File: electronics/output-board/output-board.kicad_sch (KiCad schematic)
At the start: 30 parts, among them J14 Arming switch, J19 Extra IO, J3 12V In, J4 Conn_01x02, J5 SWD Header, J6 Conn_01x02, SW1 SW_Push_Dual, U1 MAX33012EASA+, U2 LD3985M33R_SOT23, U3 STM32F105VBH6, Y1 25MHz 9pF

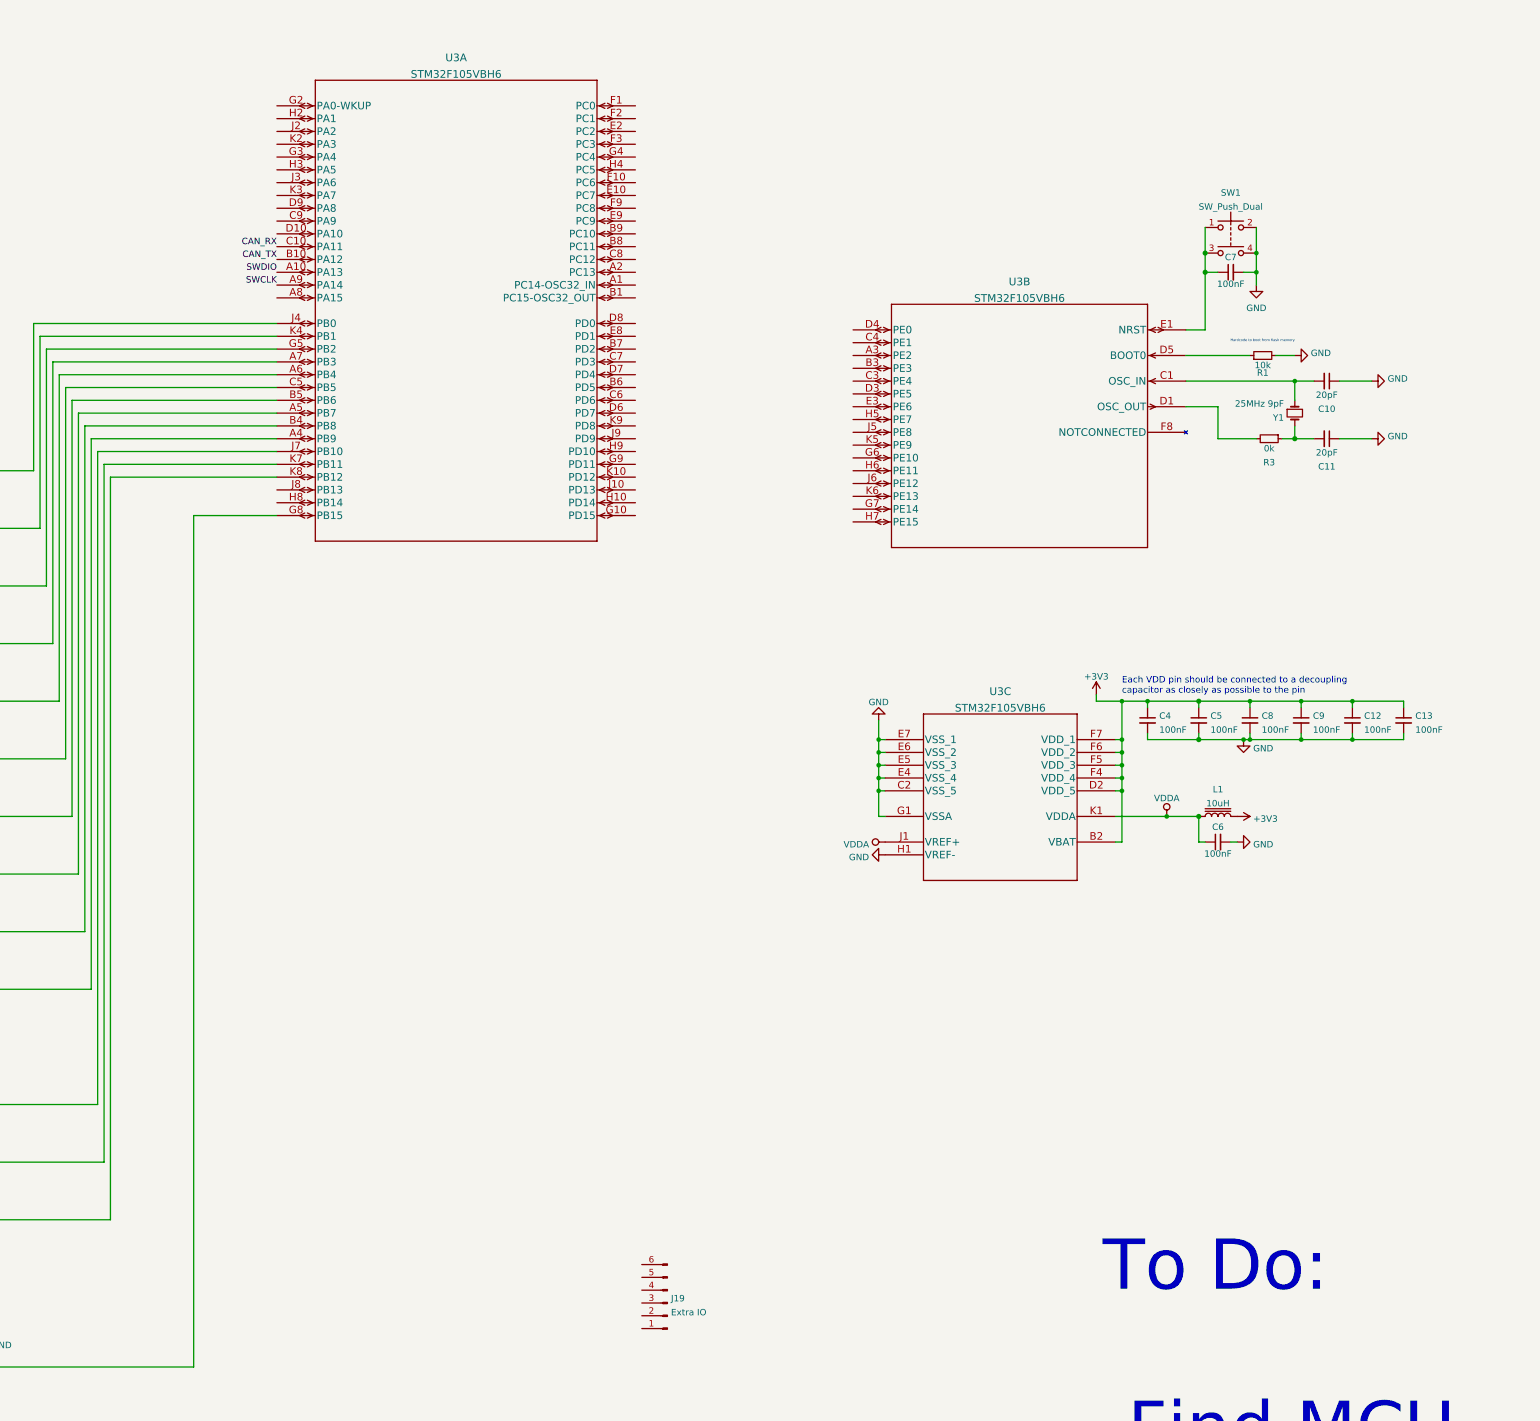
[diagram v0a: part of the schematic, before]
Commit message: Continued Laying Out Output Board
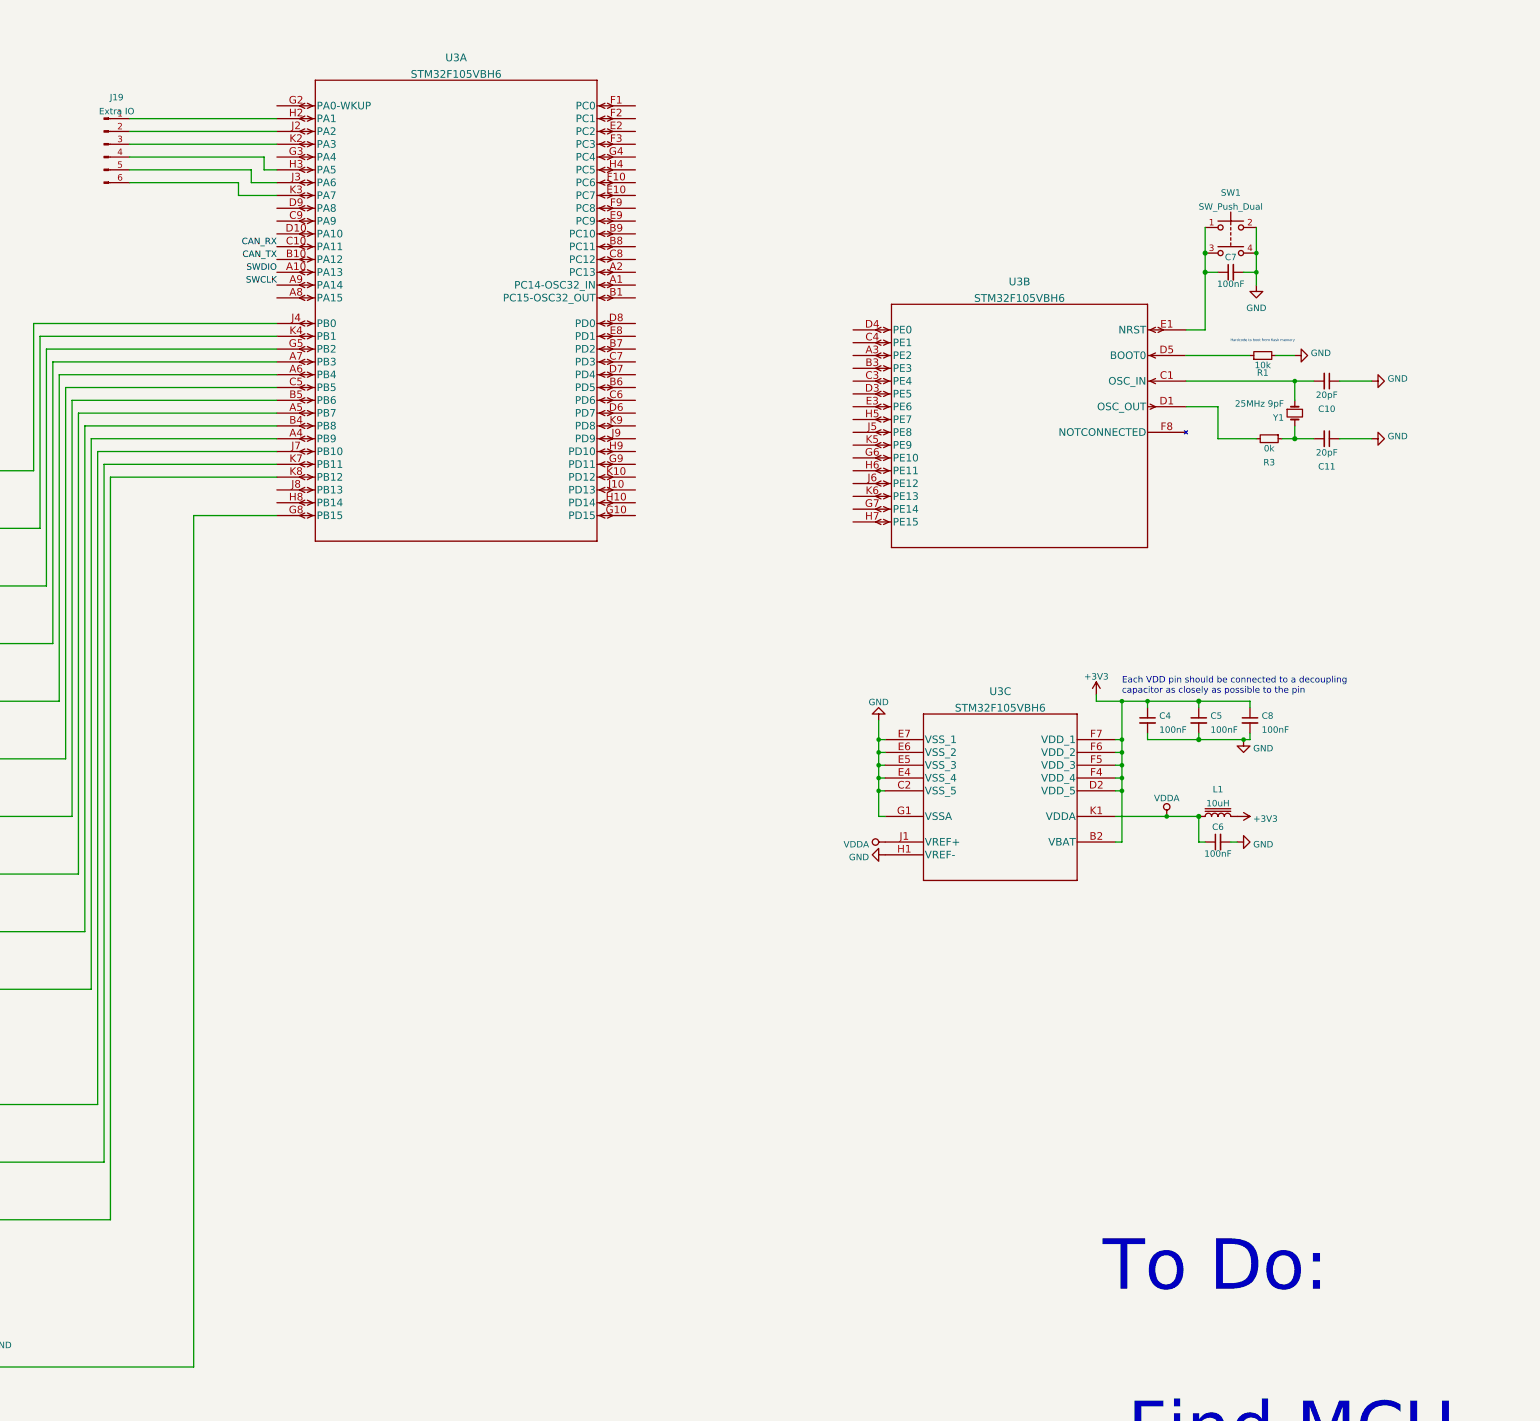
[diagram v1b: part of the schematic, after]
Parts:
- removed C12, C13, C9: 100nF, Capacitor_SMD:C_0603_1608Metric, symbol Device:C_Small
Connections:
- net at J19.1 (Pin_1): now also U3.H2 (PA1)
- net at J19.2 (Pin_2): now also U3.J2 (PA2)
- net at J19.3 (Pin_3): now also U3.K2 (PA3)
- net at J19.4 (Pin_4): now also U3.H3 (PA5)
- net at J19.5 (Pin_5): now also U3.J3 (PA6)
- net at J19.6 (Pin_6): now also U3.K3 (PA7)
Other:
- moved on the sheet: J19
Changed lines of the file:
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@@
   (junction (at 349.25 101.6) (diameter 1.016) (color 0 0 0 0))
   (junction (at 356.87 194.31) (diameter 0) (color 0 0 0 0))
-  (junction (at 358.14 186.69) (diameter 0) (color 0 0 0 0))
-  (junction (at 358.14 194.31) (diameter 0) (color 0 0 0 0))
   (junction (at 359.41 97.79) (diameter 0) (color 0 0 0 0))
   (junction (at 359.41 101.6) (diameter 0) (color 0 0 0 0))
   (junction (at 367.03 123.19) (diameter 0) (color 0 0 0 0))
   (junction (at 367.03 134.62) (diameter 1.016) (color 0 0 0 0))
-  (junction (at 368.3 186.69) (diameter 0) (color 0 0 0 0))
-  (junction (at 368.3 194.31) (diameter 0) (color 0 0 0 0))
-  (junction (at 378.46 186.69) (diameter 0) (color 0 0 0 0))
-  (junction (at 378.46 194.31) (diameter 0) (color 0 0 0 0))
   (wire (pts (xy 25.4 81.28) (xy 35.56 81.28))
     (stroke (width 0) (type solid) (color 0 0 0 0))
@@
     (stroke (width 0) (type default) (color 0 0 0 0))
   )
+  (wire (pts (xy 135.89 71.12) (xy 165.1 71.12))
+    (stroke (width 0) (type default) (color 0 0 0 0))
+  )
+  (wire (pts (xy 135.89 73.66) (xy 165.1 73.66))
+    (stroke (width 0) (type default) (color 0 0 0 0))
+  )
+  (wire (pts (xy 135.89 76.2) (xy 165.1 76.2))
+    (stroke (width 0) (type default) (color 0 0 0 0))
+  )
   (wire (pts (xy 148.59 149.86) (xy 148.59 318.77))
     (stroke (width 0) (type default) (color 0 0 0 0))
   )
+  (wire (pts (xy 157.48 83.82) (xy 135.89 83.82))
+    (stroke (width 0) (type default) (color 0 0 0 0))
+  )
+  (wire (pts (xy 157.48 86.36) (xy 157.48 83.82))
+    (stroke (width 0) (type default) (color 0 0 0 0))
+  )
+  (wire (pts (xy 160.02 81.28) (xy 135.89 81.28))
+    (stroke (width 0) (type default) (color 0 0 0 0))
+  )
+  (wire (pts (xy 160.02 83.82) (xy 160.02 81.28))
+    (stroke (width 0) (type default) (color 0 0 0 0))
+  )
+  (wire (pts (xy 162.56 78.74) (xy 135.89 78.74))
+    (stroke (width 0) (type default) (color 0 0 0 0))
+  )
+  (wire (pts (xy 162.56 81.28) (xy 162.56 78.74))
+    (stroke (width 0) (type default) (color 0 0 0 0))
+  )
+  (wire (pts (xy 165.1 81.28) (xy 162.56 81.28))
+    (stroke (width 0) (type default) (color 0 0 0 0))
+  )
+  (wire (pts (xy 165.1 83.82) (xy 160.02 83.82))
+    (stroke (width 0) (type default) (color 0 0 0 0))
+  )
+  (wire (pts (xy 165.1 86.36) (xy 157.48 86.36))
+    (stroke (width 0) (type default) (color 0 0 0 0))
+  )
   (wire (pts (xy 165.1 114.3) (xy 118.11 114.3))
     (stroke (width 0) (type default) (color 0 0 0 0))
@@
     (stroke (width 0) (type solid) (color 0 0 0 0))
   )
-  (wire (pts (xy 358.14 186.69) (xy 368.3 186.69))
-    (stroke (width 0) (type default) (color 0 0 0 0))
-  )
   (wire (pts (xy 358.14 193.04) (xy 358.14 194.31))
     (stroke (width 0) (type solid) (color 0 0 0 0))
@@
     (stroke (width 0) (type solid) (color 0 0 0 0))
   )
-  (wire (pts (xy 368.3 187.96) (xy 368.3 186.69))
-    (stroke (width 0) (type default) (color 0 0 0 0))
-  )
-  (wire (pts (xy 368.3 193.04) (xy 368.3 194.31))
-    (stroke (width 0) (type default) (color 0 0 0 0))
-  )
-  (wire (pts (xy 368.3 194.31) (xy 358.14 194.31))
-    (stroke (width 0) (type default) (color 0 0 0 0))
-  )
-  (wire (pts (xy 368.3 194.31) (xy 378.46 194.31))
-    (stroke (width 0) (type default) (color 0 0 0 0))
-  )
   (wire (pts (xy 370.84 123.19) (xy 367.03 123.19))
     (stroke (width 0) (type solid) (color 0 0 0 0))
@@
     (stroke (width 0) (type solid) (color 0 0 0 0))
   )
-  (wire (pts (xy 378.46 186.69) (xy 368.3 186.69))
-    (stroke (width 0) (type default) (color 0 0 0 0))
-  )
-  (wire (pts (xy 378.46 186.69) (xy 388.62 186.69))
-    (stroke (width 0) (type default) (color 0 0 0 0))
-  )
-  (wire (pts (xy 378.46 187.96) (xy 378.46 186.69))
-    (stroke (width 0) (type default) (color 0 0 0 0))
-  )
-  (wire (pts (xy 378.46 193.04) (xy 378.46 194.31))
-    (stroke (width 0) (type default) (color 0 0 0 0))
-  )
-  (wire (pts (xy 378.46 194.31) (xy 388.62 194.31))
-    (stroke (width 0) (type default) (color 0 0 0 0))
-  )
   (wire (pts (xy 382.27 123.19) (xy 375.92 123.19))
     (stroke (width 0) (type solid) (color 0 0 0 0))
@@
   (wire (pts (xy 382.27 134.62) (xy 375.92 134.62))
     (stroke (width 0) (type solid) (color 0 0 0 0))
-  )
-  (wire (pts (xy 388.62 187.96) (xy 388.62 186.69))
-    (stroke (width 0) (type default) (color 0 0 0 0))
-  )
-  (wire (pts (xy 388.62 193.04) (xy 388.62 194.31))
-    (stroke (width 0) (type default) (color 0 0 0 0))
   )
   (text "To Do:\n\n-Find MCU\n-Add IO Breakout\n-Finalize Connectors\n-Put together final parrts list\n-Buy parts and board"
@@
     (pin "2")
   )
-  (symbol (lib_id "Device:C_Small") (at 368.3 190.5 0) (unit 1)
-    (in_bom yes) (on_board yes)
-    (property "Reference" "C9" (id 0) (at 370.6242 189.5915 0)
-      (effects (font (size 1.27 1.27)) (justify left))
-    )
-    (property "Value" "100nF" (id 1) (at 370.6242 192.3666 0)
-      (effects (font (size 1.27 1.27)) (justify left))
-    )
-    (property "Footprint" "Capacitor_SMD:C_0603_1608Metric" (id 2) (at 368.3 190.5 0)
-      (effects (font (size 1.27 1.27)) hide)
-    )
-    (property "Datasheet" "~" (id 3) (at 368.3 190.5 0)
-      (effects (font (size 1.27 1.27)) hide)
-    )
-    (pin "1")
-    (pin "2")
-  )
   (symbol (lib_id "Device:C_Small") (at 373.38 123.19 270) (unit 1)
     (in_bom yes) (on_board yes) (fields_autoplaced)
@@
     (pin "2")
   )
-  (symbol (lib_id "Device:C_Small") (at 378.46 190.5 0) (unit 1)
-    (in_bom yes) (on_board yes)
-    (property "Reference" "C12" (id 0) (at 380.7842 189.5915 0)
-      (effects (font (size 1.27 1.27)) (justify left))
-    )
-    (property "Value" "100nF" (id 1) (at 380.7842 192.3666 0)
-      (effects (font (size 1.27 1.27)) (justify left))
-    )
-    (property "Footprint" "Capacitor_SMD:C_0603_1608Metric" (id 2) (at 378.46 190.5 0)
-      (effects (font (size 1.27 1.27)) hide)
-    )
-    (property "Datasheet" "~" (id 3) (at 378.46 190.5 0)
-      (effects (font (size 1.27 1.27)) hide)
-    )
-    (pin "1")
-    (pin "2")
-  )
-  (symbol (lib_id "Device:C_Small") (at 388.62 190.5 0) (unit 1)
-    (in_bom yes) (on_board yes)
-    (property "Reference" "C13" (id 0) (at 390.9442 189.5915 0)
-      (effects (font (size 1.27 1.27)) (justify left))
-    )
-    (property "Value" "100nF" (id 1) (at 390.9442 192.3666 0)
-      (effects (font (size 1.27 1.27)) (justify left))
-    )
-    (property "Footprint" "Capacitor_SMD:C_0603_1608Metric" (id 2) (at 388.62 190.5 0)
-      (effects (font (size 1.27 1.27)) hide)
-    )
-    (property "Datasheet" "~" (id 3) (at 388.62 190.5 0)
-      (effects (font (size 1.27 1.27)) hide)
-    )
-    (pin "1")
-    (pin "2")
-  )
   (symbol (lib_id "Device:R") (at 55.88 299.72 270) (unit 1)
     (in_bom yes) (on_board yes)
@@
     (pin "4")
   )
-  (symbol (lib_id "Connector:Conn_01x06_Male") (at 242.57 306.07 180) (unit 1)
-    (in_bom yes) (on_board yes) (fields_autoplaced)
-    (property "Reference" "J19" (id 0) (at 243.2813 305.1615 0)
-      (effects (font (size 1.27 1.27)) (justify right))
-    )
-    (property "Value" "Extra IO" (id 1) (at 243.2813 307.9366 0)
-      (effects (font (size 1.27 1.27)) (justify right))
-    )
-    (property "Footprint" "Connector_PinHeader_2.54mm:PinHeader_2x03_P2.54mm_Vertical" (id 2) (at 242.57 306.07 0)
-      (effects (font (size 1.27 1.27)) hide)
-    )
-    (property "Datasheet" "~" (id 3) (at 242.57 306.07 0)
+  (symbol (lib_id "Connector:Conn_01x06_Male") (at 130.81 76.2 0) (unit 1)
+    (in_bom yes) (on_board yes) (fields_autoplaced)
+    (property "Reference" "J19" (id 0) (at 133.3119 66.8994 0))
+    (property "Value" "Extra IO" (id 1) (at 133.3119 69.6745 0))
+    (property "Footprint" "Connector_PinHeader_2.54mm:PinHeader_2x03_P2.54mm_Vertical" (id 2) (at 130.81 76.2 0)
+      (effects (font (size 1.27 1.27)) hide)
+    )
+    (property "Datasheet" "~" (id 3) (at 130.81 76.2 0)
       (effects (font (size 1.27 1.27)) hide)
     )
@@
       (reference "C8") (unit 1) (value "100nF") (footprint "Capacitor_SMD:C_0603_1608Metric")
     )
-    (path "/6c7ff70a-85ef-4e9c-b06b-8c61c0a8b9d8"
-      (reference "C9") (unit 1) (value "100nF") (footprint "Capacitor_SMD:C_0603_1608Metric")
-    )
     (path "/a4541931-eddb-411e-a18a-57712146f98f"
       (reference "C10") (unit 1) (value "20pF") (footprint "Capacitor_SMD:C_0603_1608Metric")
@@
       (reference "C11") (unit 1) (value "20pF") (footprint "Capacitor_SMD:C_0603_1608Metric")
     )
-    (path "/688a44ec-c004-412f-bb9f-dd194ea84791"
-      (reference "C12") (unit 1) (value "100nF") (footprint "Capacitor_SMD:C_0603_1608Metric")
-    )
-    (path "/00d961ac-c8e8-4c41-92d7-0b4b5fb685a8"
-      (reference "C13") (unit 1) (value "100nF") (footprint "Capacitor_SMD:C_0603_1608Metric")
-    )
     (path "/36b6bf08-79b4-4cbd-9663-410f8ea161a3/fdaba974-f779-4819-9be4-c0a4f95a2d0b"
